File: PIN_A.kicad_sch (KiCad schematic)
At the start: 51 parts, among them J1 Conn_ARM_JTAG_SWD_10, J2 Conn_01x03_MountingPin, J3 RJ45_Hanrun_HR911105A_Horizon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, Q1 SS8050, U1 HPM5E31IPB1, U2 LAN8720A, U3 QS-301-AGS5P, U4 MLT-5020, Y2 X322525MOB4SI

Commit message: finish
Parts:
- added J15: Conn_01x03_Socket, Connector_Harwin:Harwin_M20-89003xx_1x03_P2.54mm_Horizontal, symbol Connector:Conn_01x03_Socket
- U2: footprint Package_DFN_QFN:VQFN-24-1EP_4x4mm_P0.5mm_EP2.5x2.5mm_ThermalVias -> Package_DFN_QFN:VQFN-24-1EP_4x4mm_P0.5mm_EP2.5x2.5mm
- Y2: footprint Crystal:Crystal_SMD_3225-4Pin_3.2x2.5mm -> Crystal:Crystal_SMD_2016-4Pin_2.0x1.6mm
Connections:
- net GND: now also J15.1 (Pin_1)
- net UART0.RXD: now also J15.2 (Pin_2)
- net UART0.TXD: now also J15.3 (Pin_3)

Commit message: demo第一版
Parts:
- added R62: 10R, Resistor_SMD:R_0603_1608Metric, symbol Device:R
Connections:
- net +3.3V: now also R62.1
- net ESC0.P0_RXER: now also R62.2
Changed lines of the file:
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@@
 		)
 	)
+	(label "RXER{slash}PHYAD0"
+		(at 132.08 213.36 0)
+		(effects
+			(font
+				(size 1.27 1.27)
+			)
+			(justify left bottom)
+		)
+	)
 	(label "JTAG.TDO"
 		(at 76.2 49.53 180)
@@
 	)
 	(symbol
+		(lib_id "Device:R")
+		(at 132.08 217.17 180)
+		(unit 1)
+		(body_style 1)
+		(exclude_from_sim no)
+		(in_bom yes)
+		(on_board yes)
+		(in_pos_files yes)
+		(dnp no)
+		(fields_autoplaced yes)
+		(property "Reference" "R62"
+			(at 134.62 215.8999 0)
+			(show_name no)
+			(do_not_autoplace no)
+			(effects
+				(font
+					(size 1.27 1.27)
+				)
+				(justify right)
+			)
+		)
+		(property "Value" "10R"
+			(at 134.62 218.4399 0)
+			(show_name no)
+			(do_not_autoplace no)
+			(effects
+				(font
+					(size 1.27 1.27)
+				)
+				(justify right)
+			)
+		)
+		(property "Footprint" "Resistor_SMD:R_0603_1608Metric"
+			(at 133.858 217.17 90)
+			(hide yes)
+			(show_name no)
+			(do_not_autoplace no)
+			(effects
+				(font
+					(size 1.27 1.27)
+				)
+			)
+		)
+		(property "Datasheet" ""
+			(at 132.08 217.17 0)
+			(hide yes)
+			(show_name no)
+			(do_not_autoplace no)
+			(effects
+				(font
+					(size 1.27 1.27)
+				)
+			)
+		)
+		(property "Description" "Resistor"
+			(at 132.08 217.17 0)
+			(hide yes)
+			(show_name no)
+			(do_not_autoplace no)
+			(effects
+				(font
+					(size 1.27 1.27)
+				)
+			)
+		)
+		(property "KLC_S3.3" ""
+			(at 132.08 217.17 0)
+			(hide yes)
+			(show_name no)
+			(do_not_autoplace no)
+			(effects
+				(font
+					(size 1.27 1.27)
+				)
+			)
+		)
+		(property "KLC_S4.1" ""
+			(at 132.08 217.17 0)
+			(hide yes)
+			(show_name no)
+			(do_not_autoplace no)
+			(effects
+				(font
+					(size 1.27 1.27)
+				)
+			)
+		)
+		(pin "1"
+		)
+		(pin "2"
+		)
+		(instances
+			(project "HPM5E31"
+				(path "/c97d420a-5bfd-40ab-9a74-5349ba6434d5/7e36ae8c-fe7d-4836-83fb-8a28fde457e1"
+					(reference "R62")
+					(unit 1)
+				)
+			)
+		)
+	)
+	(symbol
 		(lib_id "Connector:Conn_ARM_JTAG_SWD_10")
 		(at 54.61 46.99 0)
@@
 					(unit 1)
 				)
+			)
+		)
+	)
+	(symbol
+		(lib_id "power:+3.3V")
+		(at 132.08 220.98 180)
+		(unit 1)
+		(body_style 1)
+		(exclude_from_sim no)
+		(in_bom yes)
+		(on_board yes)
+		(in_pos_files yes)
+		(dnp no)
+		(fields_autoplaced yes)
+		(property "Reference" "#PWR0136"
+			(at 132.08 217.17 0)
+			(hide yes)
+			(show_name no)
+			(do_not_autoplace no)
+			(effects
+				(font
+					(size 1.27 1.27)
+				)
+			)
+		)
+		(property "Value" "+3.3V"
+			(at 132.08 226.06 0)
+			(show_name no)
+			(do_not_autoplace no)
+			(effects
+				(font
+					(size 1.27 1.27)
+				)
+			)
+		)
+		(property "Footprint" ""
+			(at 132.08 220.98 0)
+			(hide yes)
+			(show_name no)
+			(do_not_autoplace no)
+			(effects
+				(font
+					(size 1.27 1.27)
+				)
+			)
+		)
+		(property "Datasheet" ""
+			(at 132.08 220.98 0)
+			(hide yes)
+			(show_name no)
+			(do_not_autoplace no)
+			(effects
+				(font
+					(size 1.27 1.27)
+				)
+			)
+		)
+		(property "Description" "Power symbol creates a global label with name \"+3.3V\""
+			(at 132.08 220.98 0)
+			(hide yes)
+			(show_name no)
+			(do_not_autoplace no)
+			(effects
+				(font
+					(size 1.27 1.27)
+				)
+			)
+		)
+		(pin "1"
+		)
+		(instances
+			(project "HPM5E31"
+				(path "/c97d420a-5bfd-40ab-9a74-5349ba6434d5/7e36ae8c-fe7d-4836-83fb-8a28fde457e1"
+					(reference "#PWR0136")
+					(unit 1)
+				)

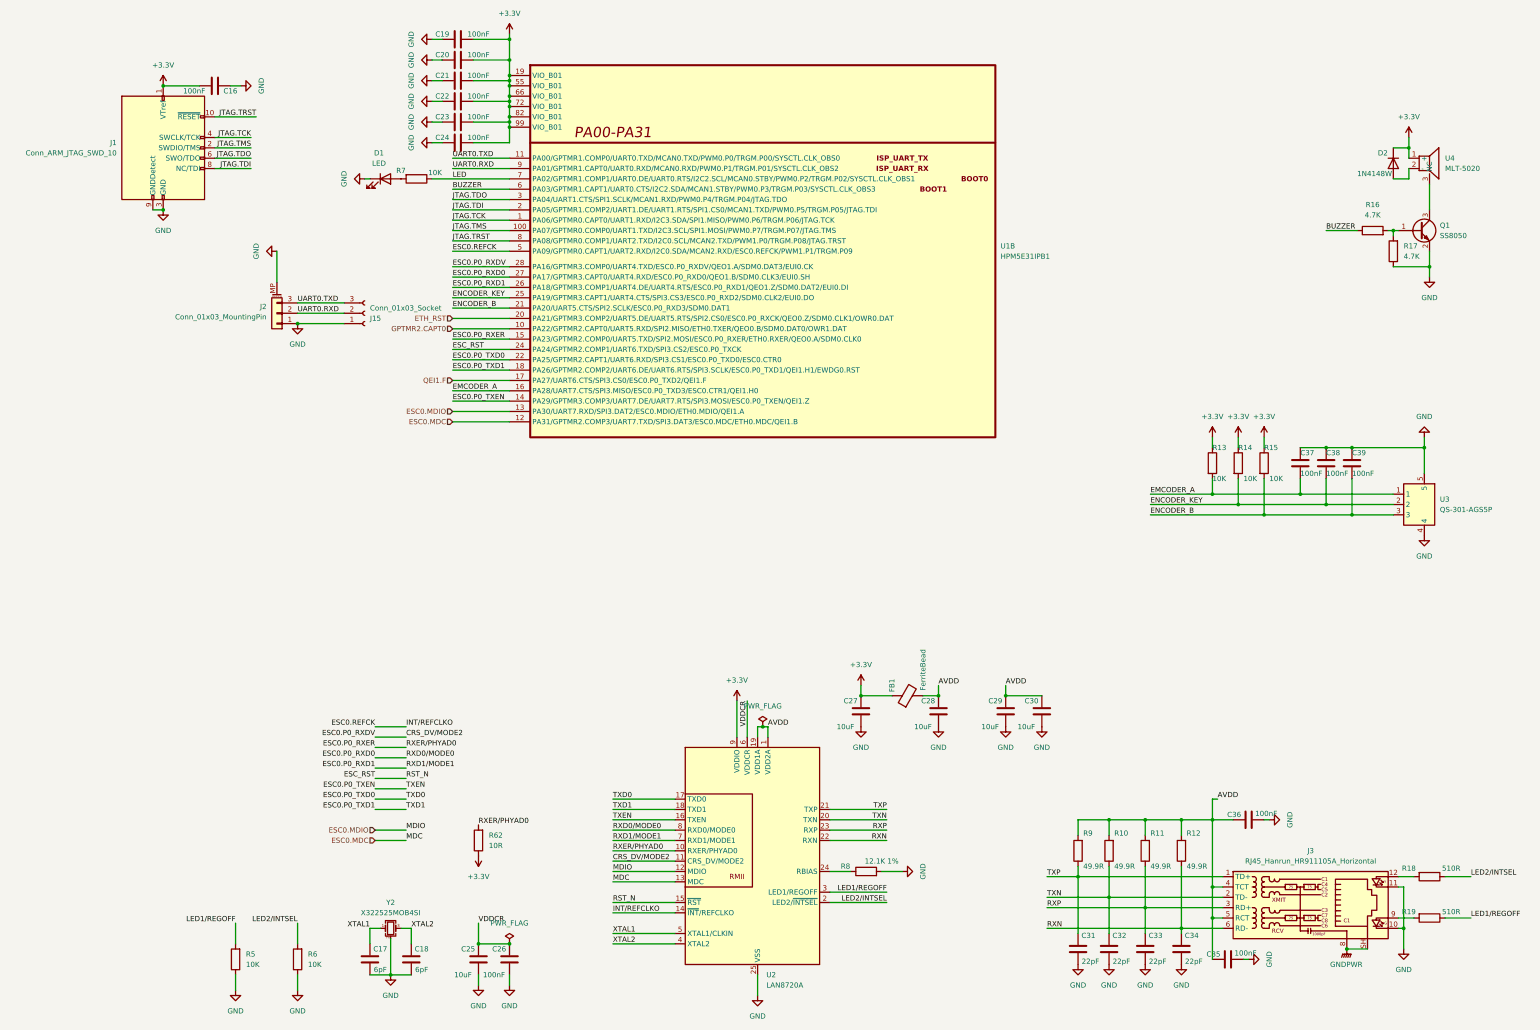
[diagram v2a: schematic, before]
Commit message: 修改错误引脚
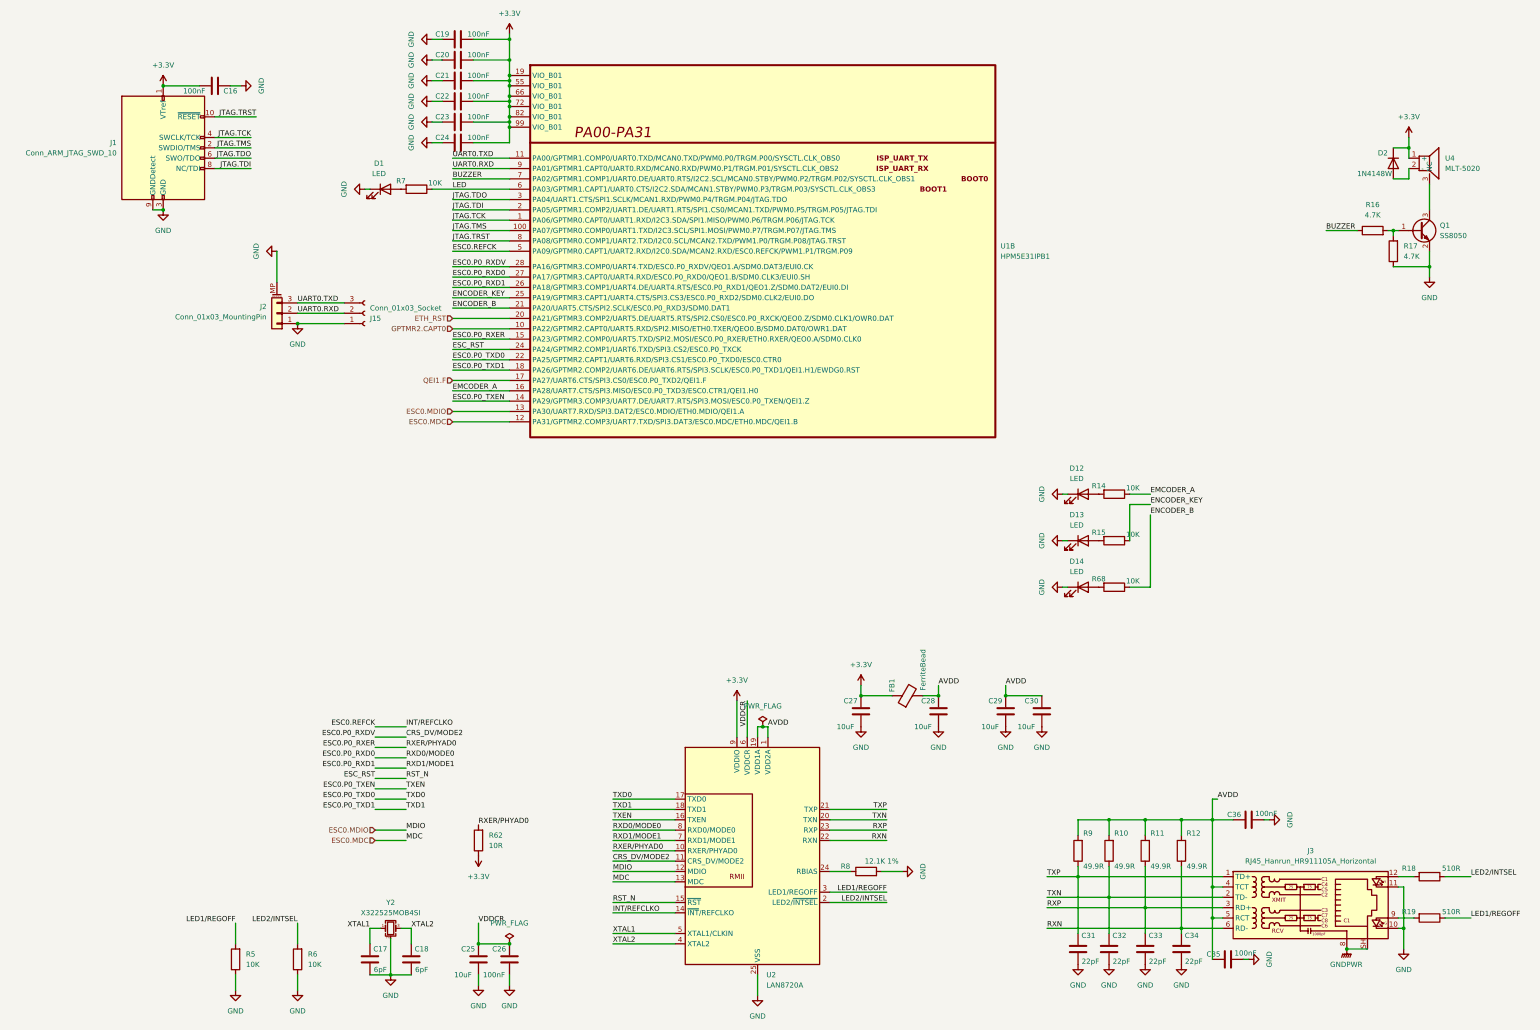
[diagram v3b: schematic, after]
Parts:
- removed C37, C38, C39: 100nF, Capacitor_SMD:C_0603_1608Metric, symbol Device:C
- removed R13: 10K, Resistor_SMD:R_0603_1608Metric, symbol Device:R
- removed U3: QS-301-AGS5P, mylib:QS-301-AGS5P_C42377853, symbol mylib:QS-301-AGS5P
- added D12, D13, D14: LED, LED_SMD:LED_0603_1608Metric, symbol Device:LED
- added R68: 10K, Resistor_SMD:R_0603_1608Metric, symbol Device:R
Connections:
- net +3.3V: no longer R14.1, R15.1
- net BUZZER: now also U1.7 (PA02/GPTMR1.COMP1/UART0.DE/UART0.RTS/I2C2.SCL/MCAN0.STBY/PWM0.P2/TRGM.P02/SYSCTL.CLK_OBS1); no longer U1.6 (PA03/GPTMR1.CAPT1/UART0.CTS/I2C2.SDA/MCAN1.STBY/PWM0.P3/TRGM.P03/SYSCTL.CLK_OBS3)
- net EMCODER_A: now also R14.1
- net ENCODER_B: now also R68.1; no longer R15.2
- net ENCODER_KEY: now also R15.1; no longer R14.2
- net GND: now also D12.1 (K), D13.1 (K), D14.1 (K)
- net LED: now also U1.6 (PA03/GPTMR1.CAPT1/UART0.CTS/I2C2.SDA/MCAN1.STBY/PWM0.P3/TRGM.P03/SYSCTL.CLK_OBS3); no longer U1.7 (PA02/GPTMR1.COMP1/UART0.DE/UART0.RTS/I2C2.SCL/MCAN0.STBY/PWM0.P2/TRGM.P02/SYSCTL.CLK_OBS1)
- new net: D13.2 (A), R15.2
- new net: D12.2 (A), R14.2
- new net: D14.2 (A), R68.2
